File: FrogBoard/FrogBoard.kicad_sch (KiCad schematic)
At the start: 44 parts, among them J1 Conn_01x10, J10 Conn_01x02, J11 Conn_01x01, J12 Conn_01x02, J13 Conn_01x01, J14 Conn_01x01, J15 Conn_01x01, J2 Conn_01x04, J3 USB_B_Micro, J4 Stickbox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

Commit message: Add LED
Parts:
- added D3: LED, LED_SMD:LED_0603_1608Metric, symbol Device:LED
- added R7: R, Resistor_SMD:R_0603_1608Metric, symbol Device:R
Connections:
- net GND: now also D3.1 (K)
- net Unused_3: no longer U1.8 (PA2)
- net Unused_4: no longer U1.9 (PA3)
- new net: R7.1, U1.8 (PA2)
- new net: D3.2 (A), R7.2
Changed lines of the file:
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@@
 	(wire
 		(pts
+			(xy 109.22 45.72) (xy 111.76 45.72)
+		)
+		(stroke
+			(width 0)
+			(type default)
+		)
+	)
+	(wire
+		(pts
 			(xy 87.63 50.8) (xy 86.36 50.8)
 		)
@@
 	(wire
 		(pts
+			(xy 86.36 45.72) (xy 101.6 45.72)
+		)
+		(stroke
+			(width 0)
+			(type default)
+		)
+	)
+	(wire
+		(pts
 			(xy 148.59 127) (xy 149.86 127)
 		)
@@
 		)
 	)
-	(global_label "Unused_3"
-		(shape bidirectional)
-		(at 86.36 45.72 0)
-		(fields_autoplaced yes)
-		(effects
-			(font
-				(size 1.27 1.27)
-			)
-			(justify left)
-		)
-		(property "Intersheetrefs" "${INTERSHEET_REFS}"
-			(at 99.5278 45.72 0)
-			(effects
-				(font
-					(size 1.27 1.27)
-				)
-				(justify left)
-				(hide yes)
-			)
-		)
-	)
 	(global_label "AX_MUX_OUT"
 		(shape input)
@@
 		)
 	)
-	(global_label "Unused_4"
-		(shape bidirectional)
-		(at 86.36 48.26 0)
-		(fields_autoplaced yes)
-		(effects
-			(font
-				(size 1.27 1.27)
-			)
-			(justify left)
-		)
-		(property "Intersheetrefs" "${INTERSHEET_REFS}"
-			(at 99.5278 48.26 0)
-			(effects
-				(font
-					(size 1.27 1.27)
-				)
-				(justify left)
-				(hide yes)
-			)
-		)
-	)
 	(global_label "Unused_5"
 		(shape bidirectional)
@@
 	)
 	(symbol
+		(lib_id "Device:R")
+		(at 105.41 45.72 90)
+		(unit 1)
+		(exclude_from_sim no)
+		(in_bom yes)
+		(on_board yes)
+		(dnp no)
+		(fields_autoplaced yes)
+		(property "Reference" "R7"
+			(at 105.41 39.37 90)
+			(effects
+				(font
+					(size 1.27 1.27)
+				)
+			)
+		)
+		(property "Value" "R"
+			(at 105.41 41.91 90)
+			(effects
+				(font
+					(size 1.27 1.27)
+				)
+			)
+		)
+		(property "Footprint" "Resistor_SMD:R_0603_1608Metric"
+			(at 105.41 47.498 90)
+			(effects
+				(font
+					(size 1.27 1.27)
+				)
+				(hide yes)
+			)
+		)
+		(property "Datasheet" "~"
+			(at 105.41 45.72 0)
+			(effects
+				(font
+					(size 1.27 1.27)
+				)
+				(hide yes)
+			)
+		)
+		(property "Description" "Resistor"
+			(at 105.41 45.72 0)
+			(effects
+				(font
+					(size 1.27 1.27)
+				)
+				(hide yes)
+			)
+		)
+		(pin "1"
+		)
+		(pin "2"
+		)
+		(instances
+			(project ""
+				(path "/70a1c624-543f-486d-b6f1-90effc8a6c8b"
+					(reference "R7")
+					(unit 1)
+				)
+			)
+		)
+	)
+	(symbol
 		(lib_id "power:+3.3V")
 		(at 19.05 30.48 180)
@@
 	)
 	(symbol
+		(lib_id "power:GND")
+		(at 111.76 53.34 0)
+		(unit 1)
+		(exclude_from_sim no)
+		(in_bom yes)
+		(on_board yes)
+		(dnp no)
+		(property "Reference" "#PWR013"
+			(at 111.76 59.69 0)
+			(effects
+				(font
+					(size 1.27 1.27)
+				)
+				(hide yes)
+			)
+		)
+		(property "Value" "GND"
+			(at 109.728 57.658 0)
+			(effects
+				(font
+					(size 1.27 1.27)
+				)
+				(justify left)
+			)
+		)
+		(property "Footprint" ""
+			(at 111.76 53.34 0)
+			(effects
+				(font
+					(size 1.27 1.27)
+				)
+				(hide yes)
+			)
+		)
+		(property "Datasheet" ""
+			(at 111.76 53.34 0)
+			(effects
+				(font
+					(size 1.27 1.27)
+				)
+				(hide yes)
+			)
+		)
+		(property "Description" "Power symbol creates a global label with name \"GND\" , ground"
+			(at 111.76 53.34 0)
+			(effects
+				(font
+					(size 1.27 1.27)
+				)
+				(hide yes)
+			)
+		)
+		(pin "1"
+		)
+		(instances
+			(project "FrogBoard"
+				(path "/70a1c624-543f-486d-b6f1-90effc8a6c8b"
+					(reference "#PWR013")
+					(unit 1)
+				)
+			)
+		)
+	)
+	(symbol
 		(lib_id "Device:R")
 		(at 153.67 77.47 0)
@@
 					(unit 1)
 				)
+			)
+		)
+	)
+	(symbol
+		(lib_id "Device:LED")
+		(at 111.76 49.53 90)
+		(unit 1)
+		(exclude_from_sim no)
+		(in_bom yes)
+		(on_board yes)
+		(dnp no)
+		(fields_autoplaced yes)
+		(property "Reference" "D3"
+			(at 115.57 49.8474 90)
+			(effects
+				(font
+					(size 1.27 1.27)
+				)
+				(justify right)
+			)
+		)
+		(property "Value" "LED"
+			(at 115.57 52.3874 90)
+			(effects
+				(font
+					(size 1.27 1.27)
+				)
+				(justify right)
+			)
+		)
+		(property "Footprint" "LED_SMD:LED_0603_1608Metric"
+			(at 111.76 49.53 0)
+			(effects
+				(font
+					(size 1.27 1.27)
+				)
+				(hide yes)
+			)
+		)
+		(property "Datasheet" "~"
+			(at 111.76 49.53 0)
+			(effects
+				(font
+					(size 1.27 1.27)
+				)
+				(hide yes)
+			)
+		)
+		(property "Description" "Light emitting diode"
+			(at 111.76 49.53 0)
+			(effects
+				(font
+					(size 1.27 1.27)
+				)
+				(hide yes)
+			)
+		)
+		(property "Sim.Pins" "1=K 2=A"
+			(at 111.76 49.53 0)
+			(effects
+				(font
+					(size 1.27 1.27)
+				)
+				(hide yes)
+			)
+		)
+		(pin "1"
+		)
+		(pin "2"
+		)
+		(instances
+			(project ""
+				(path "/70a1c624-543f-486d-b6f1-90effc8a6c8b"
+					(reference "D3")
+					(unit 1)
+				)

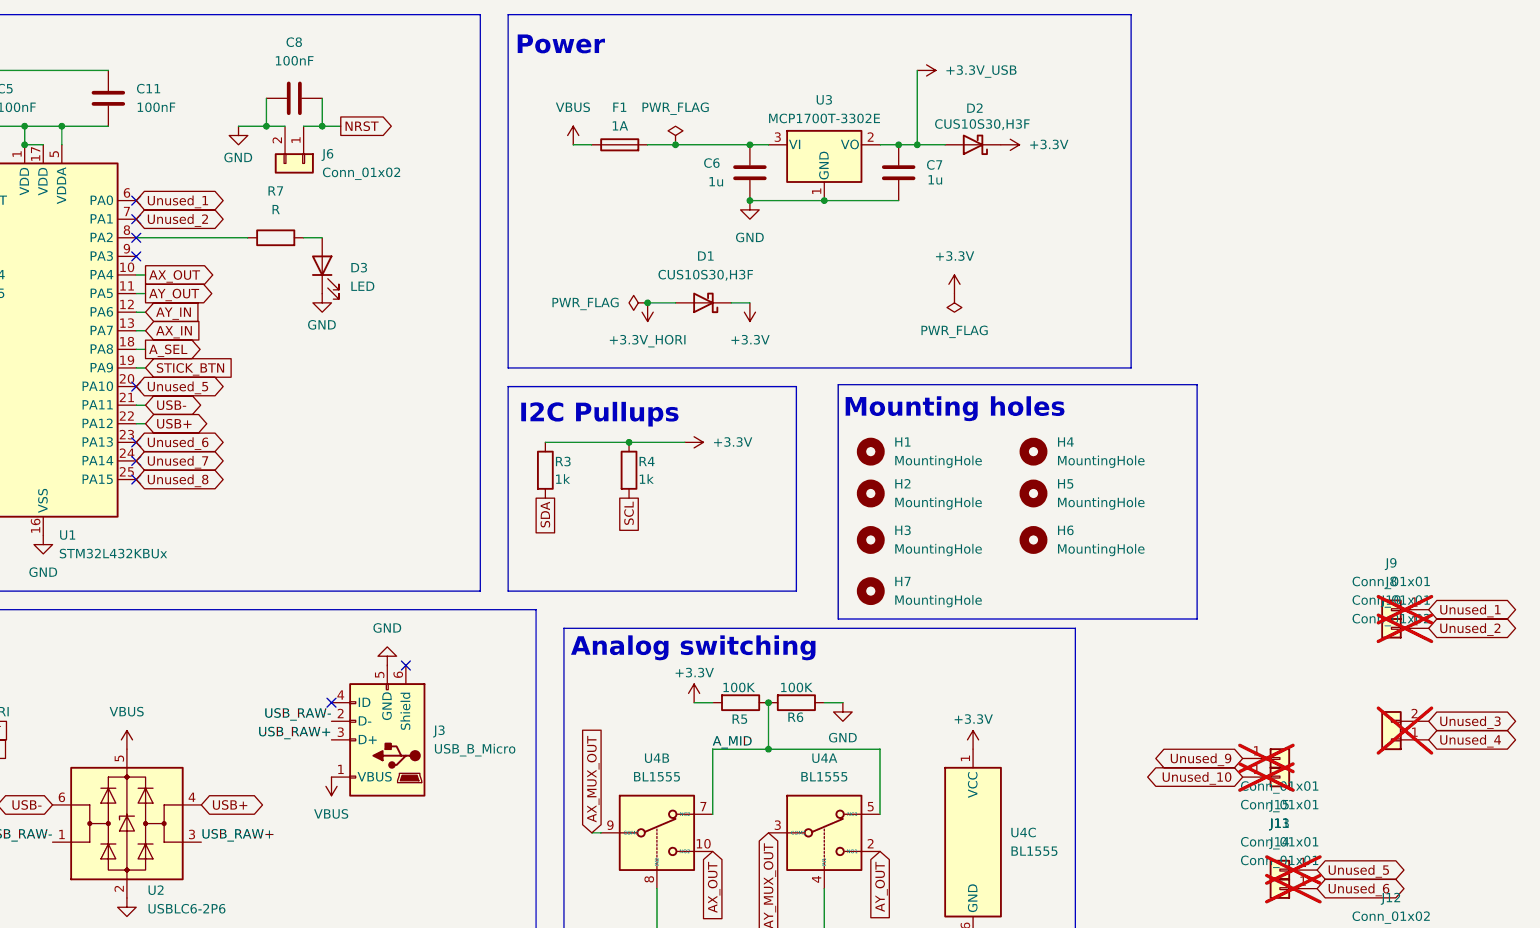
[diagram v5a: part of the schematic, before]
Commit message: adding indicator LED
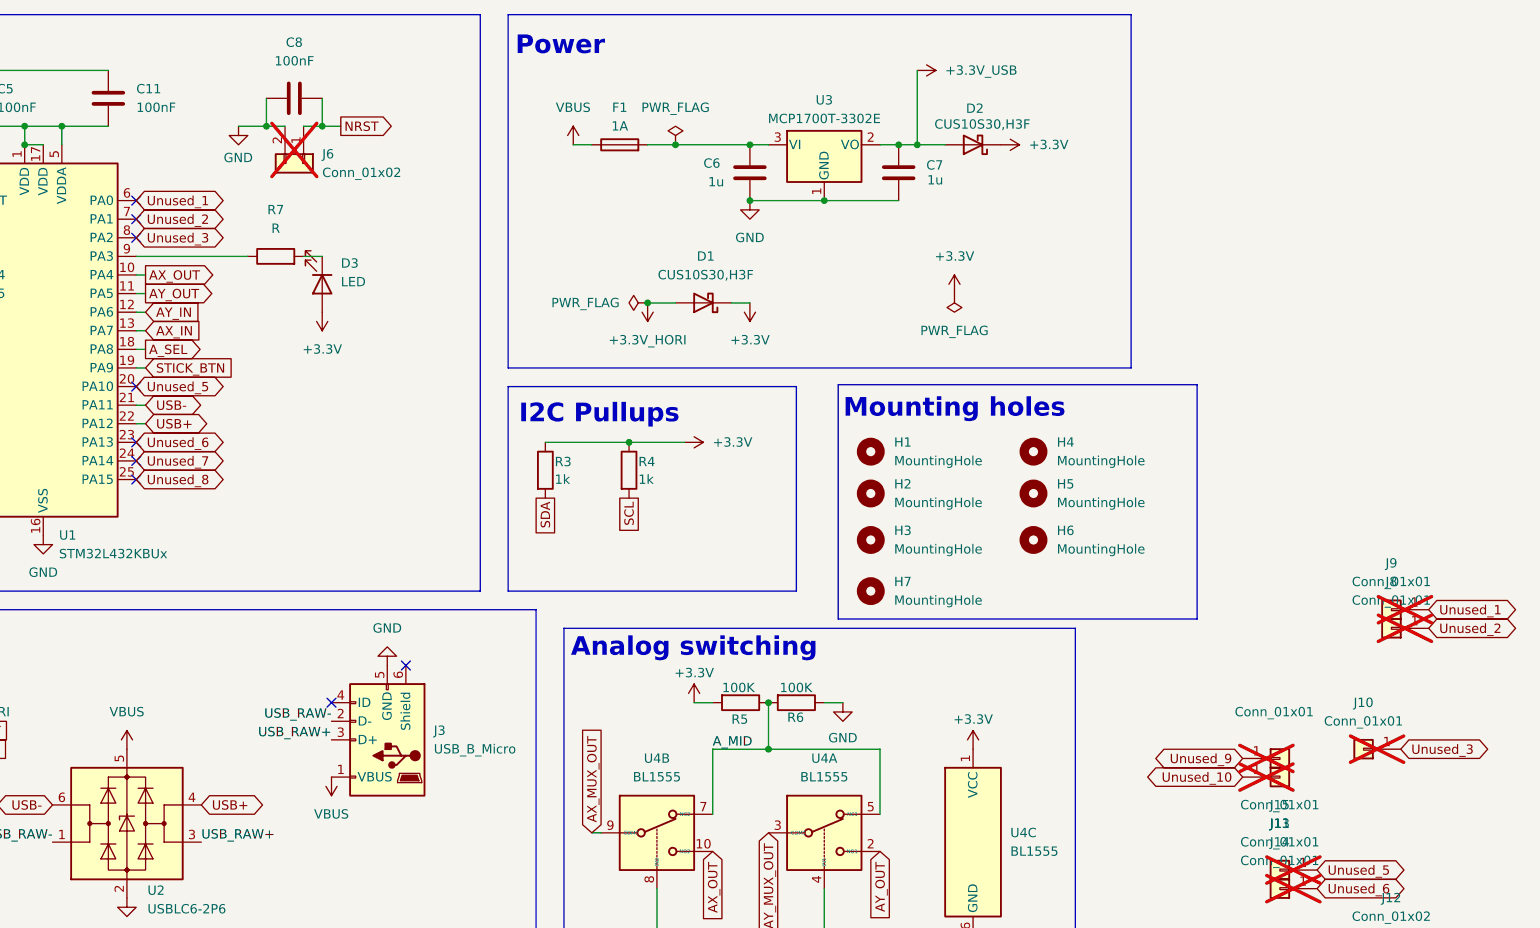
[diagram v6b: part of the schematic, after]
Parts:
- removed J10: Conn_01x02, FrogBoard_footprints:PinHeader_1x02_P1.00mm_Vertical_Neutral_No_Coutryard, symbol Connector_Generic:Conn_01x02
- added J10: Conn_01x01, FrogBoard_footprints:FrogBoard_PinHeader_1x01_P1.00mm_Vertical, symbol Connector_Generic:Conn_01x01
- J11: now left out of the parts list
- J6: now not fitted
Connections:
- net +3.3V: now also D3.2 (A)
- net GND: no longer D3.1 (K)
- net Unused_3: now also U1.8 (PA2), J10.1 (Pin_1)
- net at R7.1: now also U1.9 (PA3); no longer U1.8 (PA2)
- net at R7.2: now also D3.1 (K); no longer D3.2 (A)
- no-connect marks 12 -> 11
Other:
- moved on the sheet: D3, R7

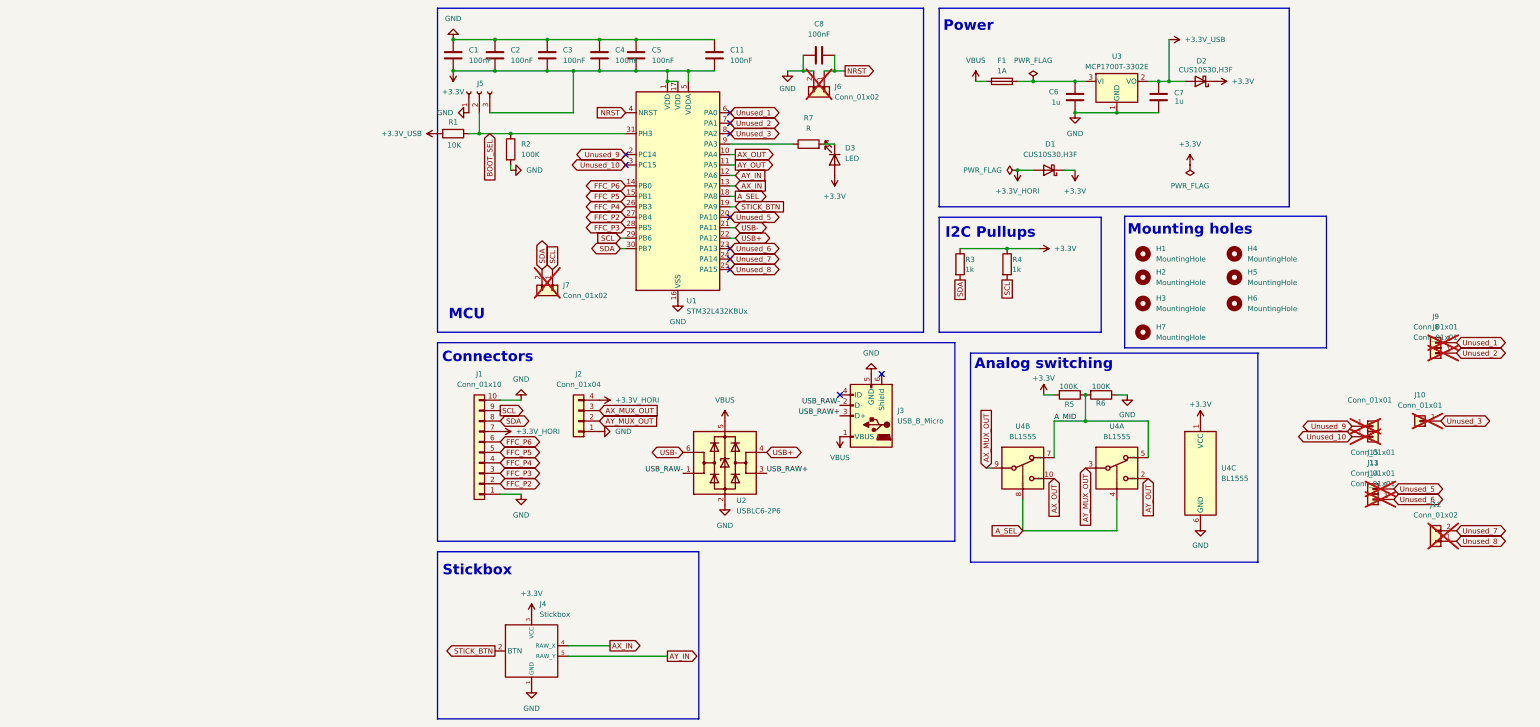
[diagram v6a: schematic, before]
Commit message: Replace micro B with USB-C connector
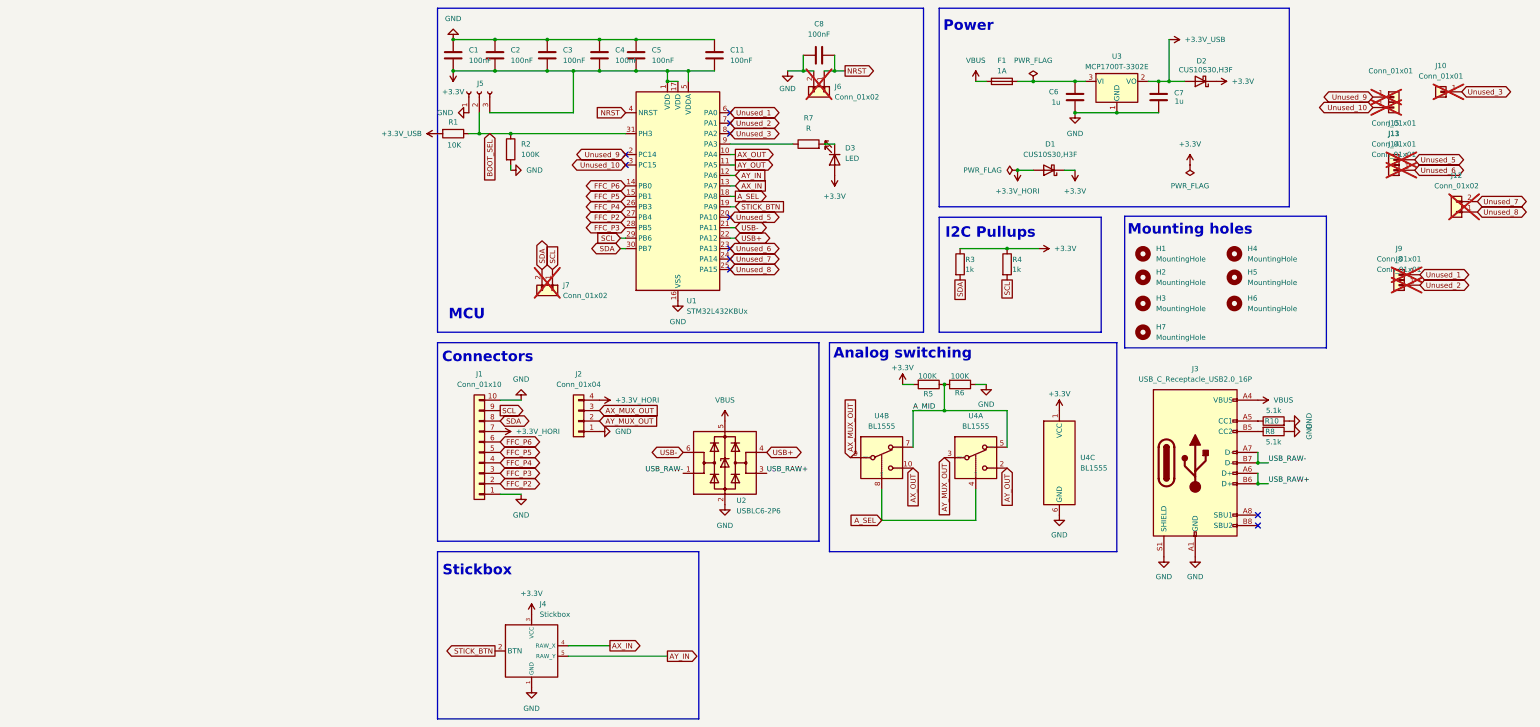
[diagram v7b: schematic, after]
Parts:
- removed J3: USB_B_Micro, FrogBoard_footprints:AMPHENOL_10118194-0001LF, symbol Connector:USB_B_Micro
- added J3: USB_C_Receptacle_USB2.0_16P, FrogBoard_footprints:CONN16_C16PIN_SHN, symbol Connector:USB_C_Receptacle_USB2.0_16P
- added R10, R8: 5.1k, Resistor_SMD:R_0603_1608Metric_Pad0.98x0.95mm_HandSolder, symbol Device:R
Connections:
- net GND: now also J3.A1 (GND), J3.A12 (GND), J3.B1 (GND), J3.B12 (GND), J3.S1 (SHIELD), R10.2, R8.1
- net USB_RAW+: now also J3.A6 (D+), J3.B6 (D+)
- net USB_RAW-: now also J3.A7 (D-), J3.B7 (D-)
- net VBUS: now also J3.A4 (VBUS), J3.A9 (VBUS), J3.B4 (VBUS), J3.B9 (VBUS)
- new net: J3.A5 (CC1), R10.1
- new net: J3.B5 (CC2), R8.2
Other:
- moved on the sheet: J10, J11, J12, J13, J14, J15, J8, J9, R5, R6, U4A, U4B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

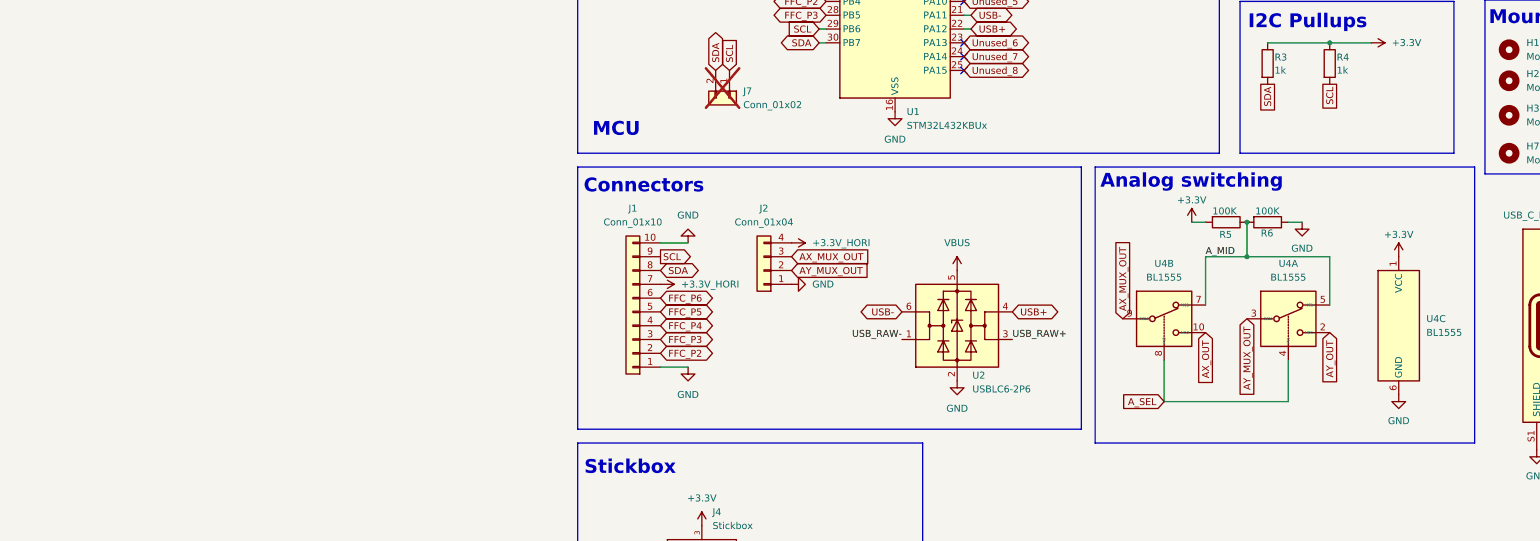
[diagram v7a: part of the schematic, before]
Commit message: Cleaned up board edge positions and layed out the main bus
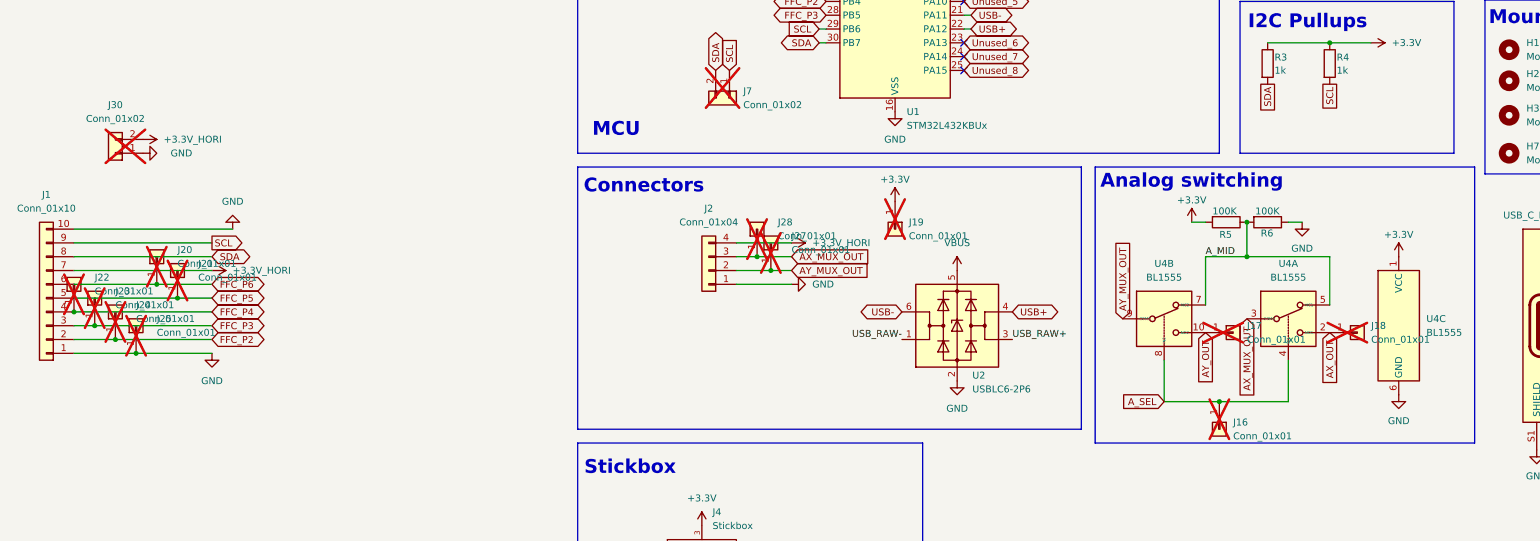
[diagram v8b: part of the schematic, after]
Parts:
- added J16, J17, J18, J19, J20, J21, J22, J23, J24, J25, J27, J28: Conn_01x01, FrogBoard_footprints:FrogBoard_PinHeader_1x01_P1.00mm_Vertical, symbol Connector_Generic:Conn_01x01
- added J30: Conn_01x02, FrogBoard_footprints:PinHeader_1x02_P1.00mm_Vertical_Neutral_No_Coutryard, symbol Connector_Generic:Conn_01x02
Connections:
- net +3.3V: now also J19.1 (Pin_1)
- net +3.3V_HORI: now also J30.2 (Pin_2)
- net AX_MUX_OUT: now also U4.3 (COM1), J28.1 (Pin_1); no longer U4.9 (COM2)
- net AX_OUT: now also U4.2 (NO1), J18.1 (Pin_1); no longer U4.10 (NO2)
- net AY_MUX_OUT: now also U4.9 (COM2), J27.1 (Pin_1); no longer U4.3 (COM1)
- net AY_OUT: now also U4.10 (NO2), J17.1 (Pin_1); no longer U4.2 (NO1)
- net A_SEL: now also J16.1 (Pin_1)
- net FFC_P2: now also J24.1 (Pin_1)
- net FFC_P3: now also J23.1 (Pin_1)
- net FFC_P4: now also J22.1 (Pin_1)
- net FFC_P5: now also J21.1 (Pin_1)
- net FFC_P6: now also J20.1 (Pin_1)
- net GND: now also J25.1 (Pin_1), J30.1 (Pin_1)
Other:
- moved on the sheet: J1, J2
